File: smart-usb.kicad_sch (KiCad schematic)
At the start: 6 parts, among them J1 Screw_Terminal_01x04, J2 Screw_Terminal_01x04, J3 USB_A, J4 USB_A, U1 MOUDLE-SEEEDUINO-XIAO-ESP32C3, U2 MIC94095YC6-TR

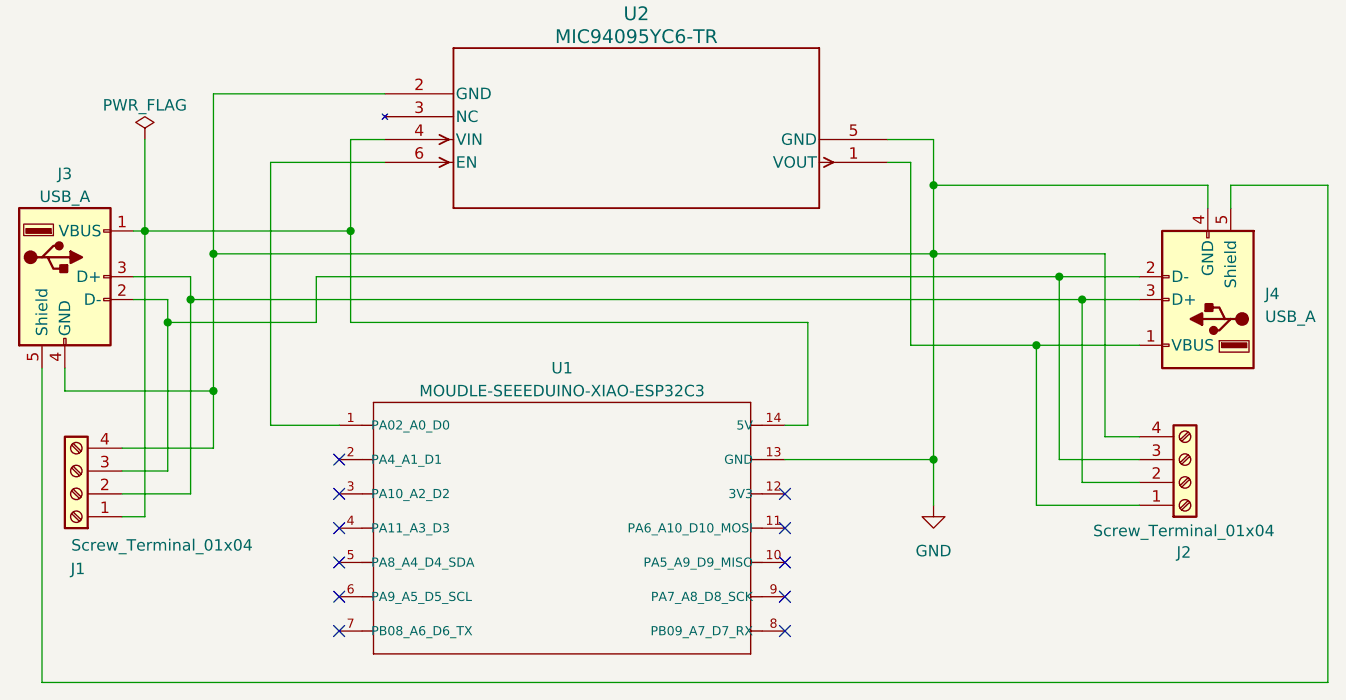
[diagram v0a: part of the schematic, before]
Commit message: feat: layout draft
* Removed optional direct solder connectors for USB in / out
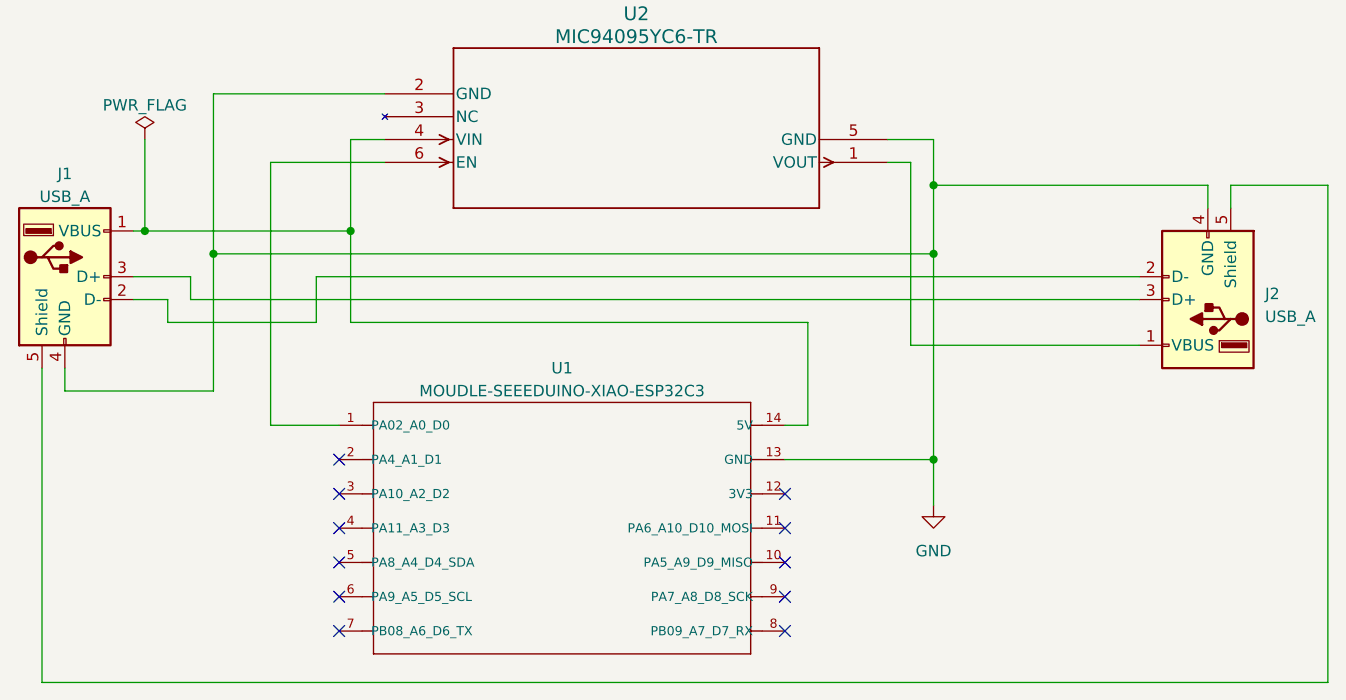
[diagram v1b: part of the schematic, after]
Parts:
- removed J1, J2: Screw_Terminal_01x04, Connector_PinSocket_2.54mm:PinSocket_1x04_P2.54mm_Vertical, symbol Connector:Screw_Terminal_01x04
- J1: renamed from J3; footprint Connector_PinSocket_2.54mm:PinSocket_1x05_P2.54mm_Vertical -> smart-usb-custom-parts:USB_AP_S_RA_Adam-Tech
- J2: renamed from J4; footprint (none) -> Connector_USB:USB_A_Molex_67643_Horizontal
- U1: footprint Seeed XIAO:MOUDLE14P-SMD-2.54-21X17.8MM -> smart-usb-custom-parts:Seeeduino XIAO-MOUDLE14P-2.54-21X17.8MM
- U2: footprint MIC94095YC6:SC-70_C6_MCH -> Package_TO_SOT_SMD:SOT-363_SC-70-6_Handsoldering
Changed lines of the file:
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@@
   (junction (at 78.74 52.07) (diameter 0) (color 0 0 0 0)
   )
-  (junction (at 182.88 59.69) (diameter 0) (color 0 0 0 0)
-  )
-  (junction (at 180.34 57.15) (diameter 0) (color 0 0 0 0)
-  )
   (junction (at 166.37 46.99) (diameter 0) (color 0 0 0 0)
   )
-  (junction (at 86.36 69.85) (diameter 0) (color 0 0 0 0)
-  )
-  (junction (at 83.82 59.69) (diameter 0) (color 0 0 0 0)
-  )
   (junction (at 166.37 54.61) (diameter 0) (color 0 0 0 0)
   )
-  (junction (at 81.28 62.23) (diameter 0) (color 0 0 0 0)
-  )
   (junction (at 86.36 54.61) (diameter 0) (color 0 0 0 0)
-  )
-  (junction (at 177.8 64.77) (diameter 0) (color 0 0 0 0)
   )
   (no_connect (at 149.86 85.09))
@@
     (stroke (width 0) (type default))
   )
-  (wire (pts (xy 83.82 59.69) (xy 83.82 81.28))
-    (stroke (width 0) (type default))
-  )
   (wire (pts (xy 163.83 64.77) (xy 163.83 44.45))
     (stroke (width 0) (type default))
   )
-  (wire (pts (xy 182.88 59.69) (xy 83.82 59.69))
-    (stroke (width 0) (type default))
-  )
-  (wire (pts (xy 177.8 64.77) (xy 163.83 64.77))
+  (wire (pts (xy 83.82 59.69) (xy 189.23 59.69))
+    (stroke (width 0) (type default))
+  )
+  (wire (pts (xy 163.83 64.77) (xy 189.23 64.77))
     (stroke (width 0) (type default))
   )
@@
     (stroke (width 0) (type default))
   )
-  (wire (pts (xy 86.36 76.2) (xy 86.36 69.85))
-    (stroke (width 0) (type default))
-  )
   (wire (pts (xy 152.4 62.23) (xy 152.4 73.66))
     (stroke (width 0) (type default))
   )
-  (wire (pts (xy 182.88 80.01) (xy 182.88 59.69))
-    (stroke (width 0) (type default))
-  )
   (wire (pts (xy 86.36 54.61) (xy 166.37 54.61))
     (stroke (width 0) (type default))
   )
-  (wire (pts (xy 78.74 52.07) (xy 78.74 83.82))
-    (stroke (width 0) (type default))
-  )
   (wire (pts (xy 149.86 77.47) (xy 166.37 77.47))
     (stroke (width 0) (type default))
   )
-  (wire (pts (xy 189.23 64.77) (xy 177.8 64.77))
-    (stroke (width 0) (type default))
-  )
-  (wire (pts (xy 189.23 77.47) (xy 180.34 77.47))
-    (stroke (width 0) (type default))
-  )
   (wire (pts (xy 101.6 41.91) (xy 101.6 52.07))
     (stroke (width 0) (type default))
@@
     (stroke (width 0) (type default))
   )
-  (wire (pts (xy 189.23 82.55) (xy 177.8 82.55))
-    (stroke (width 0) (type default))
-  )
-  (wire (pts (xy 78.74 83.82) (xy 76.2 83.82))
-    (stroke (width 0) (type default))
-  )
-  (wire (pts (xy 189.23 80.01) (xy 182.88 80.01))
-    (stroke (width 0) (type default))
-  )
   (wire (pts (xy 161.29 41.91) (xy 166.37 41.91))
     (stroke (width 0) (type default))
@@
     (stroke (width 0) (type default))
   )
-  (wire (pts (xy 182.88 59.69) (xy 189.23 59.69))
-    (stroke (width 0) (type default))
-  )
-  (wire (pts (xy 177.8 82.55) (xy 177.8 64.77))
-    (stroke (width 0) (type default))
-  )
-  (wire (pts (xy 189.23 74.93) (xy 185.42 74.93))
-    (stroke (width 0) (type default))
-  )
   (wire (pts (xy 69.85 69.85) (xy 86.36 69.85))
     (stroke (width 0) (type default))
@@
     (stroke (width 0) (type default))
   )
-  (wire (pts (xy 76.2 76.2) (xy 86.36 76.2))
-    (stroke (width 0) (type default))
-  )
   (wire (pts (xy 67.31 67.31) (xy 67.31 102.235))
     (stroke (width 0) (type default))
@@
     (stroke (width 0) (type default))
   )
-  (wire (pts (xy 76.2 78.74) (xy 81.28 78.74))
-    (stroke (width 0) (type default))
-  )
   (wire (pts (xy 67.31 102.235) (xy 210.185 102.235))
     (stroke (width 0) (type default))
   )
-  (wire (pts (xy 180.34 57.15) (xy 97.79 57.15))
+  (wire (pts (xy 97.79 57.15) (xy 189.23 57.15))
     (stroke (width 0) (type default))
   )
@@
     (stroke (width 0) (type default))
   )
-  (wire (pts (xy 180.34 57.15) (xy 189.23 57.15))
-    (stroke (width 0) (type default))
-  )
-  (wire (pts (xy 185.42 74.93) (xy 185.42 54.61))
-    (stroke (width 0) (type default))
-  )
   (wire (pts (xy 166.37 46.99) (xy 166.37 54.61))
     (stroke (width 0) (type default))
@@
     (stroke (width 0) (type default))
   )
-  (wire (pts (xy 166.37 54.61) (xy 185.42 54.61))
-    (stroke (width 0) (type default))
-  )
   (wire (pts (xy 166.37 77.47) (xy 166.37 82.55))
     (stroke (width 0) (type default))
   )
-  (wire (pts (xy 180.34 77.47) (xy 180.34 57.15))
-    (stroke (width 0) (type default))
-  )
   (wire (pts (xy 97.79 57.15) (xy 97.79 62.23))
     (stroke (width 0) (type default))
@@
     (stroke (width 0) (type default))
   )
-  (wire (pts (xy 81.28 62.23) (xy 81.28 78.74))
-    (stroke (width 0) (type default))
-  )
   (wire (pts (xy 152.4 73.66) (xy 149.86 73.66))
     (stroke (width 0) (type default))
@@
   )
   (wire (pts (xy 78.74 41.91) (xy 78.74 52.07))
-    (stroke (width 0) (type default))
-  )
-  (wire (pts (xy 76.2 81.28) (xy 83.82 81.28))
     (stroke (width 0) (type default))
   )
@@
       (effects (font (size 1.524 1.524)))
     )
-    (property "Footprint" "MIC94095YC6:SC-70_C6_MCH" (at 105.41 36.83 0)
+    (property "Footprint" "Package_TO_SOT_SMD:SOT-363_SC-70-6_Handsoldering" (at 105.41 36.83 0)
       (effects (font (size 1.27 1.27) italic) hide)
     )
@@
   (symbol (lib_id "Connector:USB_A") (at 69.85 57.15 0) (unit 1)
     (in_bom yes) (on_board yes) (dnp no) (fields_autoplaced)
-    (property "Reference" "J3" (at 69.85 45.72 0)
+    (property "Reference" "J1" (at 69.85 45.72 0)
       (effects (font (size 1.27 1.27)))
     )
@@
       (effects (font (size 1.27 1.27)))
     )
-    (property "Footprint" "Connector_PinSocket_2.54mm:PinSocket_1x05_P2.54mm_Vertical" (at 73.66 58.42 0)
+    (property "Footprint" "smart-usb-custom-parts:USB_AP_S_RA_Adam-Tech" (at 73.66 58.42 0)
       (effects (font (size 1.27 1.27)) hide)
     )
@@
       (project "smart-usb"
         (path "/13506c2f-fb9c-4e71-8be4-ef9715402314"
-          (reference "J3") (unit 1)
-        )
-      )
-    )
-  )
-  (symbol (lib_id "Connector:Screw_Terminal_01x04") (at 71.12 81.28 180) (unit 1)
-    (in_bom yes) (on_board yes) (dnp no)
-    (property "Reference" "J1" (at 71.2978 89.6112 0)
-      (effects (font (size 1.27 1.27)))
-    )
-    (property "Value" "Screw_Terminal_01x04" (at 80.645 86.995 0)
-      (effects (font (size 1.27 1.27)))
-    )
-    (property "Footprint" "Connector_PinSocket_2.54mm:PinSocket_1x04_P2.54mm_Vertical" (at 71.12 81.28 0)
-      (effects (font (size 1.27 1.27)) hide)
-    )
-    (property "Datasheet" "~" (at 71.12 81.28 0)
-      (effects (font (size 1.27 1.27)) hide)
-    )
-    (pin "1")
-    (pin "2")
-    (pin "3")
-    (pin "4")
-    (instances
-      (project "smart-usb"
-        (path "/13506c2f-fb9c-4e71-8be4-ef9715402314"
           (reference "J1") (unit 1)
         )
@@
     )
   )
-  (symbol (lib_id "Connector:Screw_Terminal_01x04") (at 194.31 80.01 0) (mirror x) (unit 1)
-    (in_bom yes) (on_board yes) (dnp no)
-    (property "Reference" "J2" (at 194.183 87.7824 0)
-      (effects (font (size 1.27 1.27)))
-    )
-    (property "Value" "Screw_Terminal_01x04" (at 194.183 85.3948 0)
-      (effects (font (size 1.27 1.27)))
-    )
-    (property "Footprint" "Connector_PinSocket_2.54mm:PinSocket_1x04_P2.54mm_Vertical" (at 194.31 80.01 0)
-      (effects (font (size 1.27 1.27)) hide)
-    )
-    (property "Datasheet" "~" (at 194.31 80.01 0)
-      (effects (font (size 1.27 1.27)) hide)
-    )
-    (pin "1")
-    (pin "2")
-    (pin "3")
-    (pin "4")
-    (instances
-      (project "smart-usb"
-        (path "/13506c2f-fb9c-4e71-8be4-ef9715402314"
-          (reference "J2") (unit 1)
-        )
-      )
-    )
-  )
   (symbol (lib_id "Connector:USB_A") (at 196.85 59.69 180) (unit 1)
     (in_bom yes) (on_board yes) (dnp no) (fields_autoplaced)
-    (property "Reference" "J4" (at 203.2 59.055 0)
+    (property "Reference" "J2" (at 203.2 59.055 0)
       (effects (font (size 1.27 1.27)) (justify right))
     )
@@
       (effects (font (size 1.27 1.27)) (justify right))
     )
-    (property "Footprint" "" (at 193.04 58.42 0)
+    (property "Footprint" "Connector_USB:USB_A_Molex_67643_Horizontal" (at 193.04 58.42 0)
       (effects (font (size 1.27 1.27)) hide)
     )
@@
       (project "smart-usb"
         (path "/13506c2f-fb9c-4e71-8be4-ef9715402314"
-          (reference "J4") (unit 1)
+          (reference "J2") (unit 1)
         )
       )
@@
       (effects (font (size 1.27 1.27)))
     )
-    (property "Footprint" "Seeed XIAO:MOUDLE14P-SMD-2.54-21X17.8MM" (at 125.73 85.09 0)
+    (property "Footprint" "smart-usb-custom-parts:Seeeduino XIAO-MOUDLE14P-2.54-21X17.8MM" (at 125.73 85.09 0)
       (effects (font (size 1.27 1.27)) (justify bottom) hide)
     )

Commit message: feat: fab submission candidate
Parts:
- added H1, H2, H3, H4: MountingHole, MountingHole:MountingHole_3.2mm_M3, symbol Mechanical:MountingHole
- added J10, J6: V-, Connector_PinHeader_2.54mm:PinHeader_1x01_P2.54mm_Vertical, symbol Connector_Generic:Conn_01x01
- added J3, J7: V+, Connector_PinHeader_2.54mm:PinHeader_1x01_P2.54mm_Vertical, symbol Connector_Generic:Conn_01x01
- added J4, J8: D-, Connector_PinHeader_2.54mm:PinHeader_1x01_P2.54mm_Vertical, symbol Connector_Generic:Conn_01x01
- added J5, J9: D+, Connector_PinHeader_2.54mm:PinHeader_1x01_P2.54mm_Vertical, symbol Connector_Generic:Conn_01x01
- added U3: WeMos_D1_mini, Module:WEMOS_D1_mini_light, symbol MCU_Module:WeMos_D1_mini
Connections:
- net GND: now also J10.1 (Pin_1), J6.1 (Pin_1), U3.10 (GND)
- net at J2.1 (VBUS), U2.1 (VOUT): now also J7.1 (Pin_1)
- net at J1.1 (VBUS), U1.14 (5V), U2.4 (VIN): now also J3.1 (Pin_1), U3.9 (5V)
- net at U1.1 (PA02_A0_D0), U2.6 (EN): now also U3.11 (D4)
- net at J1.2 (D-), J2.2 (D-): now also J4.1 (Pin_1), J8.1 (Pin_1)
- net at J1.3 (D+), J2.3 (D+): now also J5.1 (Pin_1), J9.1 (Pin_1)
- no-connect marks 11 -> 24
